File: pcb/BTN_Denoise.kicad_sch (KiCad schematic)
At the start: 5 parts, among them U12 74LVC2G14

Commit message: Schema & PCB: reconect output of charger from SNS to VBAT
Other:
- company: (none) -> Author: Petr Malaník
- title: (none) -> Kratos pack
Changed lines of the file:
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@@
 (kicad_sch (version 20211123) (generator eeschema)
   (paper "A4")
+  (title_block
+    (title "Kratos pack")
+    (date "2022-07-01")
+    (rev "v1.1")
+    (company "Author: Petr Malaník")
+  )
   (junction (at 137.16 87.63) (diameter 1.016) (color 0 0 0 0)
   )

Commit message: PCB: change footprint of resistors and capacitors to smaller version
After first version is apparent that smaller footprint used on some
resistors are big enough for manual soldering. Because of this was
exchanged for custom smaller version.

In current version pull-up resistor of reset circuit is not connected,
because is mend to be removed in future.
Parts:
- C27: footprint Capacitor_SMD:C_0603_1608Metric -> TCY_passives:C_0603_1608Metric
- R35: footprint Resistor_SMD:R_0603_1608Metric -> TCY_passives:R_0603_1608Metric
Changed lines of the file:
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@@
       (effects (font (size 1.27 1.27)) (justify left))
     )
-    (property "Footprint" "Capacitor_SMD:C_0603_1608Metric" (id 2) (at 118.4402 95.25 0)
+    (property "Footprint" "TCY_passives:C_0603_1608Metric" (id 2) (at 118.4402 95.25 0)
       (effects (font (size 1.27 1.27)) hide)
     )
@@
     (property "Reference" "R35" (id 0) (at 109.22 89.9922 90))
     (property "Value" "1k" (id 1) (at 113.03 89.7636 90))
-    (property "Footprint" "Resistor_SMD:R_0603_1608Metric" (id 2) (at 111.76 85.852 90)
+    (property "Footprint" "TCY_passives:R_0603_1608Metric" (id 2) (at 111.76 85.852 90)
       (effects (font (size 1.27 1.27)) hide)
     )

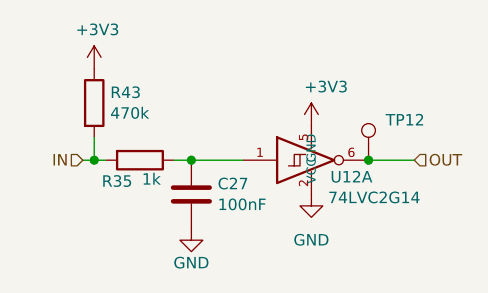
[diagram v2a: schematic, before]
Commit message: Schema & PCB: Fix USB detection by MCU and USB converter, hide GND labels
USB detection circuit is now connected only to MCU.
Converter from USB to UART (CP2102) is directly connected to VBUS.
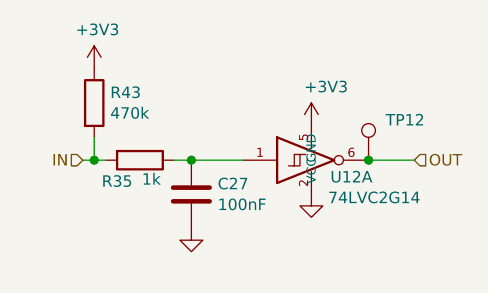
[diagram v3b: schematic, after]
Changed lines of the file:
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@@
       (effects (font (size 1.27 1.27)) hide)
     )
-    (property "Value" "GND" (id 1) (at 117.475 99.06 0))
+    (property "Value" "GND" (id 1) (at 117.475 99.06 0)
+      (effects (font (size 1.27 1.27)) hide)
+    )
     (property "Footprint" "" (id 2) (at 117.475 95.25 0)
       (effects (font (size 1.27 1.27)) hide)
@@
       (effects (font (size 1.27 1.27)) hide)
     )
-    (property "Value" "GND" (id 1) (at 130.81 96.52 0))
+    (property "Value" "GND" (id 1) (at 130.81 96.52 0)
+      (effects (font (size 1.27 1.27)) hide)
+    )
     (property "Footprint" "" (id 2) (at 130.81 91.44 0)
       (effects (font (size 1.27 1.27)) hide)

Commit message: Schema: Removed intended ILIM connection, mirror connectors, fix typos
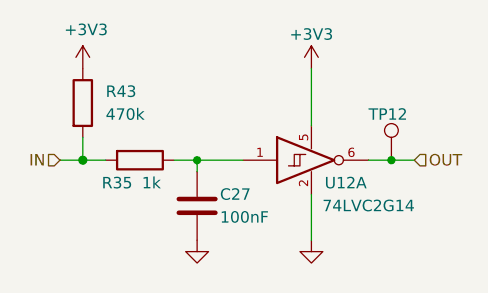
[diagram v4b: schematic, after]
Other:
- moved on the sheet: C27, R43, TP12
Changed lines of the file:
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@@
     (company "Author: Petr Malaník")
   )
-  (junction (at 137.16 87.63) (diameter 1.016) (color 0 0 0 0)
+  (junction (at 118.11 87.63) (diameter 0) (color 0 0 0 0)
   )
-  (junction (at 106.68 87.63) (diameter 1.016) (color 0 0 0 0)
+  (junction (at 105.41 87.63) (diameter 1.016) (color 0 0 0 0)
   )
-  (junction (at 117.475 87.63) (diameter 1.016) (color 0 0 0 0)
+  (junction (at 139.7 87.63) (diameter 0) (color 0 0 0 0)
   )
-  (wire (pts (xy 106.68 87.63) (xy 107.95 87.63))
+  (wire (pts (xy 130.81 91.44) (xy 130.81 96.52))
+    (stroke (width 0) (type default) (color 0 0 0 0))
+  )
+  (wire (pts (xy 105.41 87.63) (xy 107.95 87.63))
     (stroke (width 0) (type solid) (color 0 0 0 0))
   )
-  (wire (pts (xy 142.24 87.63) (xy 137.16 87.63))
+  (wire (pts (xy 142.24 87.63) (xy 139.7 87.63))
     (stroke (width 0) (type solid) (color 0 0 0 0))
   )
-  (wire (pts (xy 115.57 87.63) (xy 117.475 87.63))
+  (wire (pts (xy 115.57 87.63) (xy 118.11 87.63))
     (stroke (width 0) (type solid) (color 0 0 0 0))
   )
-  (wire (pts (xy 106.68 85.09) (xy 106.68 87.63))
+  (wire (pts (xy 118.11 87.63) (xy 118.11 88.9))
+    (stroke (width 0) (type default) (color 0 0 0 0))
+  )
+  (wire (pts (xy 137.16 87.63) (xy 139.7 87.63))
     (stroke (width 0) (type solid) (color 0 0 0 0))
   )
-  (wire (pts (xy 105.41 87.63) (xy 106.68 87.63))
+  (wire (pts (xy 105.41 85.09) (xy 105.41 87.63))
     (stroke (width 0) (type solid) (color 0 0 0 0))
   )
-  (wire (pts (xy 117.475 87.63) (xy 123.19 87.63))
+  (wire (pts (xy 130.81 77.47) (xy 130.81 83.82))
+    (stroke (width 0) (type default) (color 0 0 0 0))
+  )
+  (wire (pts (xy 102.87 87.63) (xy 105.41 87.63))
     (stroke (width 0) (type solid) (color 0 0 0 0))
   )
-  (hierarchical_label "IN" (shape input) (at 105.41 87.63 180)
+  (wire (pts (xy 118.11 87.63) (xy 123.19 87.63))
+    (stroke (width 0) (type solid) (color 0 0 0 0))
+  )
+  (hierarchical_label "IN" (shape input) (at 102.87 87.63 180)
     (effects (font (size 1.27 1.27)) (justify right))
   )
@@
     (effects (font (size 1.27 1.27)) (justify left))
   )
-  (symbol (lib_id "power:GND") (at 117.475 95.25 0) (unit 1)
+  (symbol (lib_id "power:GND") (at 118.11 96.52 0) (unit 1)
     (in_bom yes) (on_board yes)
-    (property "Reference" "#PWR083" (id 0) (at 117.475 101.6 0)
+    (property "Reference" "#PWR083" (id 0) (at 118.11 102.87 0)
       (effects (font (size 1.27 1.27)) hide)
     )
-    (property "Value" "GND" (id 1) (at 117.475 99.06 0)
+    (property "Value" "GND" (id 1) (at 118.11 100.33 0)
       (effects (font (size 1.27 1.27)) hide)
     )
-    (property "Footprint" "" (id 2) (at 117.475 95.25 0)
+    (property "Footprint" "" (id 2) (at 118.11 96.52 0)
       (effects (font (size 1.27 1.27)) hide)
     )
-    (property "Datasheet" "" (id 3) (at 117.475 95.25 0)
+    (property "Datasheet" "" (id 3) (at 118.11 96.52 0)
       (effects (font (size 1.27 1.27)) hide)
     )
@@
   (symbol (lib_id "74xGxx:74LVC2G14") (at 130.81 87.63 0) (unit 1)
     (in_bom yes) (on_board yes)
-    (property "Reference" "U12" (id 0) (at 135.255 89.516 0))
-    (property "Value" "74LVC2G14" (id 1) (at 137.795 91.8145 0))
+    (property "Reference" "U12" (id 0) (at 134.62 90.17 0))
+    (property "Value" "74LVC2G14" (id 1) (at 137.16 92.71 0))
     (property "Footprint" "Package_TO_SOT_SMD:SOT-363_SC-70-6" (id 2) (at 130.81 87.63 0)
       (effects (font (size 1.27 1.27)) hide)
@@
     (pin "4")
   )
-  (symbol (lib_id "Device:C") (at 117.475 91.44 0) (unit 1)
+  (symbol (lib_id "Device:C") (at 118.11 92.71 0) (unit 1)
     (in_bom yes) (on_board yes)
-    (property "Reference" "C27" (id 0) (at 120.396 90.2716 0)
+    (property "Reference" "C27" (id 0) (at 120.65 91.44 0)
       (effects (font (size 1.27 1.27)) (justify left))
     )
-    (property "Value" "100nF" (id 1) (at 120.396 92.583 0)
+    (property "Value" "100nF" (id 1) (at 120.65 93.98 0)
       (effects (font (size 1.27 1.27)) (justify left))
     )
-    (property "Footprint" "TCY_passives:C_0603_1608Metric" (id 2) (at 118.4402 95.25 0)
+    (property "Footprint" "TCY_passives:C_0603_1608Metric" (id 2) (at 119.0752 96.52 0)
       (effects (font (size 1.27 1.27)) hide)
     )
-    (property "Datasheet" "~" (id 3) (at 117.475 91.44 0)
+    (property "Datasheet" "~" (id 3) (at 118.11 92.71 0)
       (effects (font (size 1.27 1.27)) hide)
     )
@@
     (pin "2")
   )
-  (symbol (lib_id "power:+3V3") (at 106.68 77.47 0) (unit 1)
+  (symbol (lib_id "power:+3V3") (at 105.41 77.47 0) (unit 1)
     (in_bom yes) (on_board yes)
-    (property "Reference" "#PWR0109" (id 0) (at 106.68 81.28 0)
+    (property "Reference" "#PWR0109" (id 0) (at 105.41 81.28 0)
       (effects (font (size 1.27 1.27)) hide)
     )
-    (property "Value" "+3V3" (id 1) (at 107.0483 73.1456 0))
-    (property "Footprint" "" (id 2) (at 106.68 77.47 0)
+    (property "Value" "+3V3" (id 1) (at 105.7783 73.1456 0))
+    (property "Footprint" "" (id 2) (at 105.41 77.47 0)
       (effects (font (size 1.27 1.27)) hide)
     )
-    (property "Datasheet" "" (id 3) (at 106.68 77.47 0)
+    (property "Datasheet" "" (id 3) (at 105.41 77.47 0)
       (effects (font (size 1.27 1.27)) hide)
     )
@@
   (symbol (lib_id "Device:R") (at 111.76 87.63 270) (unit 1)
     (in_bom yes) (on_board yes)
-    (property "Reference" "R35" (id 0) (at 109.22 89.9922 90))
-    (property "Value" "1k" (id 1) (at 113.03 89.7636 90))
+    (property "Reference" "R35" (id 0) (at 109.22 90.17 90))
+    (property "Value" "1k" (id 1) (at 113.03 90.17 90))
     (property "Footprint" "TCY_passives:R_0603_1608Metric" (id 2) (at 111.76 85.852 90)
       (effects (font (size 1.27 1.27)) hide)
@@
     (pin "2")
   )
-  (symbol (lib_id "Connector:TestPoint") (at 137.16 87.63 0) (unit 1)
+  (symbol (lib_id "Connector:TestPoint") (at 139.7 87.63 0) (unit 1)
     (in_bom yes) (on_board yes)
-    (property "Reference" "TP12" (id 0) (at 139.065 83.185 0)
+    (property "Reference" "TP12" (id 0) (at 137.16 82.55 0)
       (effects (font (size 1.27 1.27)) (justify left))
     )
-    (property "Value" "TestPoint" (id 1) (at 139.065 86.995 0)
+    (property "Value" "TestPoint" (id 1) (at 141.605 86.995 0)
       (effects (font (size 1.27 1.27)) (justify left) hide)
     )
-    (property "Footprint" "TCY_connectors:TestPoint_Pad_D0.5mm" (id 2) (at 142.24 87.63 0)
+    (property "Footprint" "TCY_connectors:TestPoint_Pad_D0.5mm" (id 2) (at 144.78 87.63 0)
       (effects (font (size 1.27 1.27)) hide)
     )
-    (property "Datasheet" "~" (id 3) (at 142.24 87.63 0)
+    (property "Datasheet" "~" (id 3) (at 144.78 87.63 0)
       (effects (font (size 1.27 1.27)) hide)
     )
     (pin "1")
   )
-  (symbol (lib_id "Device:R") (at 106.68 81.28 0) (unit 1)
+  (symbol (lib_id "Device:R") (at 105.41 81.28 0) (unit 1)
     (in_bom yes) (on_board yes)
-    (property "Reference" "R43" (id 0) (at 108.4581 80.1306 0)
+    (property "Reference" "R43" (id 0) (at 107.95 80.01 0)
       (effects (font (size 1.27 1.27)) (justify left))
     )
-    (property "Value" "470k" (id 1) (at 108.4581 82.4293 0)
+    (property "Value" "470k" (id 1) (at 107.95 82.55 0)
       (effects (font (size 1.27 1.27)) (justify left))
     )
-    (property "Footprint" "TCY_passives:R_0603_1608Metric" (id 2) (at 104.902 81.28 90)
+    (property "Footprint" "TCY_passives:R_0603_1608Metric" (id 2) (at 103.632 81.28 90)
       (effects (font (size 1.27 1.27)) hide)
     )
-    (property "Datasheet" "~" (id 3) (at 106.68 81.28 0)
+    (property "Datasheet" "~" (id 3) (at 105.41 81.28 0)
       (effects (font (size 1.27 1.27)) hide)
     )
@@
     (pin "2")
   )
-  (symbol (lib_id "power:+3V3") (at 130.81 83.82 0) (unit 1)
+  (symbol (lib_id "power:+3V3") (at 130.81 77.47 0) (unit 1)
     (in_bom yes) (on_board yes)
-    (property "Reference" "#PWR085" (id 0) (at 130.81 87.63 0)
+    (property "Reference" "#PWR085" (id 0) (at 130.81 81.28 0)
       (effects (font (size 1.27 1.27)) hide)
     )
-    (property "Value" "+3V3" (id 1) (at 132.4483 79.4956 0))
-    (property "Footprint" "" (id 2) (at 130.81 83.82 0)
+    (property "Value" "+3V3" (id 1) (at 130.81 73.66 0))
+    (property "Footprint" "" (id 2) (at 130.81 77.47 0)
       (effects (font (size 1.27 1.27)) hide)
     )
-    (property "Datasheet" "" (id 3) (at 130.81 83.82 0)
+    (property "Datasheet" "" (id 3) (at 130.81 77.47 0)
       (effects (font (size 1.27 1.27)) hide)
     )
     (pin "1")
   )
-  (symbol (lib_id "power:GND") (at 130.81 91.44 0) (unit 1)
+  (symbol (lib_id "power:GND") (at 130.81 96.52 0) (unit 1)
     (in_bom yes) (on_board yes)
-    (property "Reference" "#PWR084" (id 0) (at 130.81 97.79 0)
+    (property "Reference" "#PWR084" (id 0) (at 130.81 102.87 0)
       (effects (font (size 1.27 1.27)) hide)
     )
-    (property "Value" "GND" (id 1) (at 130.81 96.52 0)
+    (property "Value" "GND" (id 1) (at 130.81 101.6 0)
       (effects (font (size 1.27 1.27)) hide)
     )
-    (property "Footprint" "" (id 2) (at 130.81 91.44 0)
+    (property "Footprint" "" (id 2) (at 130.81 96.52 0)
       (effects (font (size 1.27 1.27)) hide)
     )
-    (property "Datasheet" "" (id 3) (at 130.81 91.44 0)
+    (property "Datasheet" "" (id 3) (at 130.81 96.52 0)
       (effects (font (size 1.27 1.27)) hide)
     )
